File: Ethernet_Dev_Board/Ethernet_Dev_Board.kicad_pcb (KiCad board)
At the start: 2 copper layers, 120 parts, among them J101 Power In, J401 TAG-CONNECT_NL_10-POS_LEGS, Q201 PMV48XPA2R, U101 AZ1117, U102 74AUP1T08GWH, U103 1.2V, U201 WIZNET_W5500, U401 74AUP1T08GWH, U402 ESP32-WROOM-32E, Y201 25MHz, Y301 25MHz

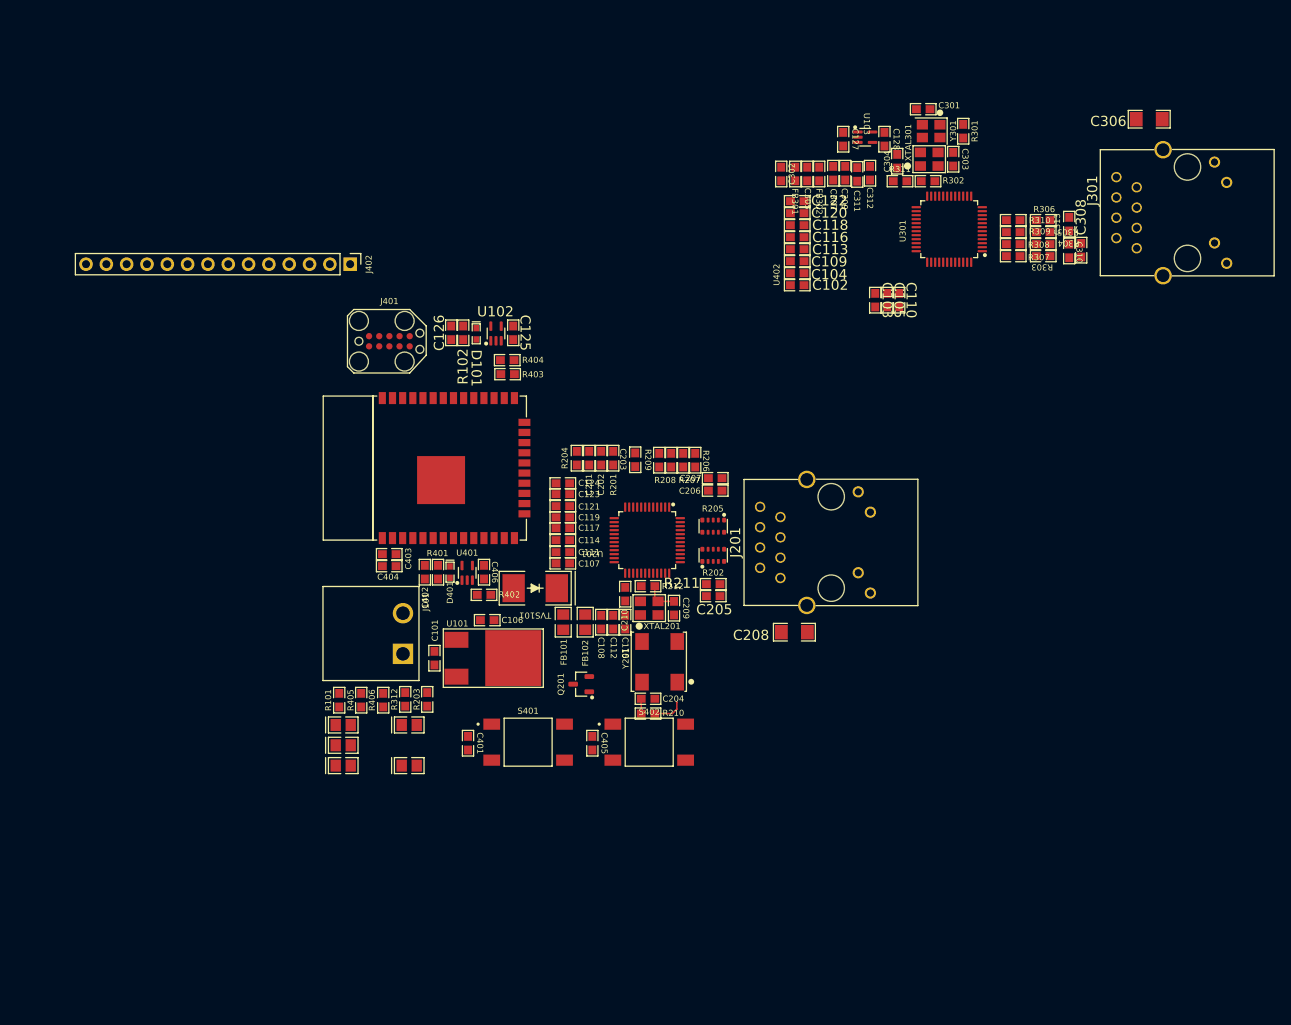
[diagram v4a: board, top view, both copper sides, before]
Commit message: Removed unnecessary nets. Beginning board routing
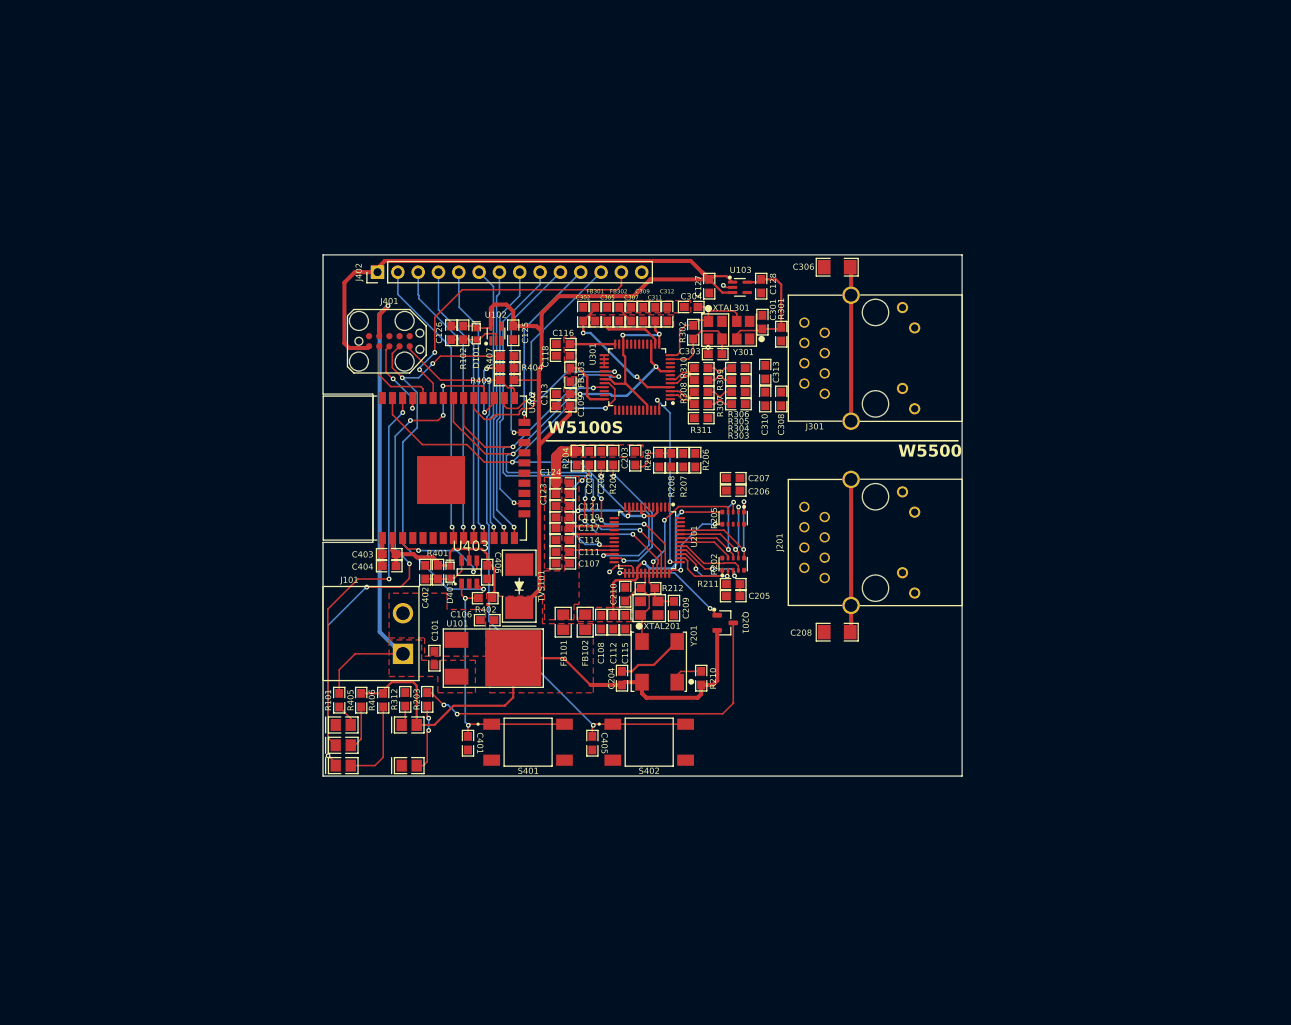
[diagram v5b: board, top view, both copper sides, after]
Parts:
- removed C102, C103, C104, C105: 22uF, RG_Capacitors_SMD:0603
- removed C110, C120, C122: 0.1uF, RG_Capacitors_SMD:0603
- removed U401: 74AUP1T08GWH, RG_TO_SOT_SMD:SOT23-5P65
- added FB103: ~, RG_Resistors_SMD:0603, F.Cu at (108.9, 60.4)
- added R407: 10k, RG_Resistors_SMD:0603, F.Cu at (101.0, 58.0)
- added U403: 74LVC1G11W6, RG_TO_SOT_SMD:SOT23-6, F.Cu at (96.2, 85.0)
- moved C306 43.2 mm to (142.2, 46.9)
- moved R307 43.2 mm to (125.2, 64.0)
- moved R308 43.2 mm to (125.2, 62.5)
- moved R309 43.2 mm to (125.2, 61.0)
- moved R310 43.2 mm to (125.2, 59.5)
- moved U301 43.2 mm to (117.2, 60.6)
- moved J301 43.0 mm to (145.1, 58.2)
- moved R303 42.4 mm to (129.9, 64.0)
- moved R304 42.4 mm to (129.9, 62.5)
- moved R305 42.4 mm to (129.9, 61.0)
- moved R306 42.4 mm to (129.9, 59.5)
- moved C310 42.3 mm to (133.2, 63.4)
- moved C313 42.3 mm to (133.2, 60.0)
- moved C308 41.9 mm to (135.2, 63.4)
- moved R311 38.7 mm to (125.2, 65.8), turned to 180 degrees
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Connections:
- C109 pad 1: +3.3VA -> +3.3V
- C113 pad 1: +3.3VA -> +3.3V
- C116 pad 1: +3.3VA -> +3.3VA2
- C118 pad 1: +3.3VA -> +3.3VA2
- U103 pad 2: GNDS -> GND1
- U301 pad 15: +3.3VA -> +3.3V
- U301 pad 16: GNDS -> GND1
- U301 pad 24: +3.3VD -> +3.3VA2
- U301 pad 36: +3.3VD -> +3.3VA2
- U301 pad 8: +3.3VA -> +3.3V
- XTAL201 pad 2: GNDS -> GND1
- XTAL301 pad 2: GNDS -> GND1
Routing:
- net +3.3V: track 1.85 -> 267.0 mm, vias 0 -> 2
- net IO0: track 0.00 -> 78.8 mm, vias 0 -> 2
- net MOSI: track 0.00 -> 68.8 mm, vias 0 -> 5
- net Net-(U402-IO17): track 0.00 -> 66.8 mm, vias 0 -> 6
- net SCK: track 0.00 -> 63.3 mm, vias 0 -> 5
- net +5V: track 0.00 -> 61.3 mm, vias 0 -> 1
- net MISO: track 0.00 -> 59.9 mm, vias 0 -> 5
- net RST: track 0.00 -> 54.3 mm, vias 0 -> 3
- net Net-(U402-IO22): track 0.00 -> 50.5 mm, vias 0 -> 2
- net Net-(Q201-D): track 0.00 -> 50.2 mm, vias 0 -> 2
- net IO21: track 0.00 -> 38.4 mm, vias 0 -> 2
- net IO32: track 0.00 -> 36.3 mm, vias 0 -> 1
- net IO33: track 0.00 -> 35.6 mm, vias 0 -> 1
- net IO12: track 0.00 -> 35.4 mm, vias 0 -> 1
- net IO25: track 0.00 -> 35.2 mm, vias 0 -> 1
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- added copper zone on F.Cu, net +1.2VD
- added copper zone on F.Cu, net +1.2VO
- added copper zone on F.Cu, net +3.3V
- added copper zone on F.Cu, net +3.3VA
- added copper zone on F.Cu, net +3.3VA2
- added copper zone on F.Cu, net +3.3VD
- added copper zone on F.Cu, net +5V
- added copper zone on F.Cu, net GND1
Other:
- board outline added: 79.9 x 65.2 mm
- board text added: "W5100S"
- board text added: "W5500"

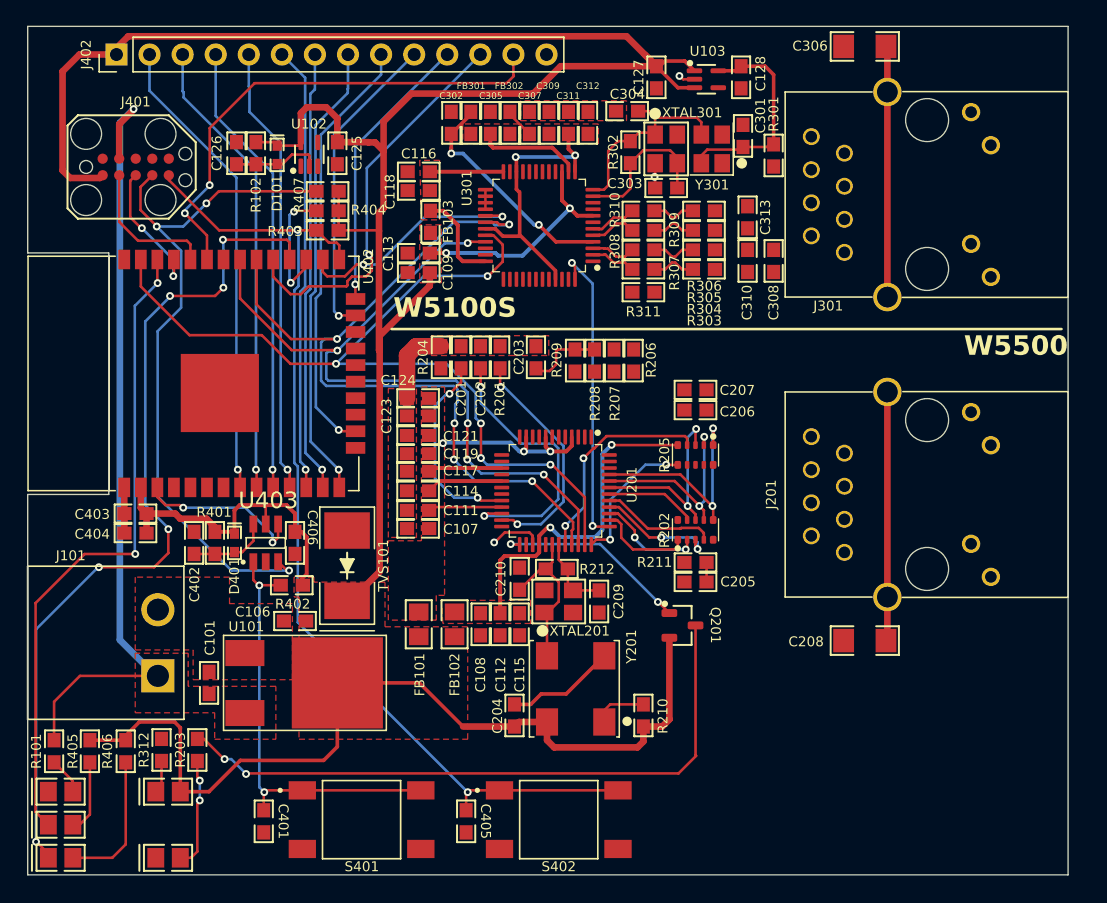
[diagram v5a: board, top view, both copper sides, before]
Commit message: Finished first version of routing the board. Also adjusted some nets
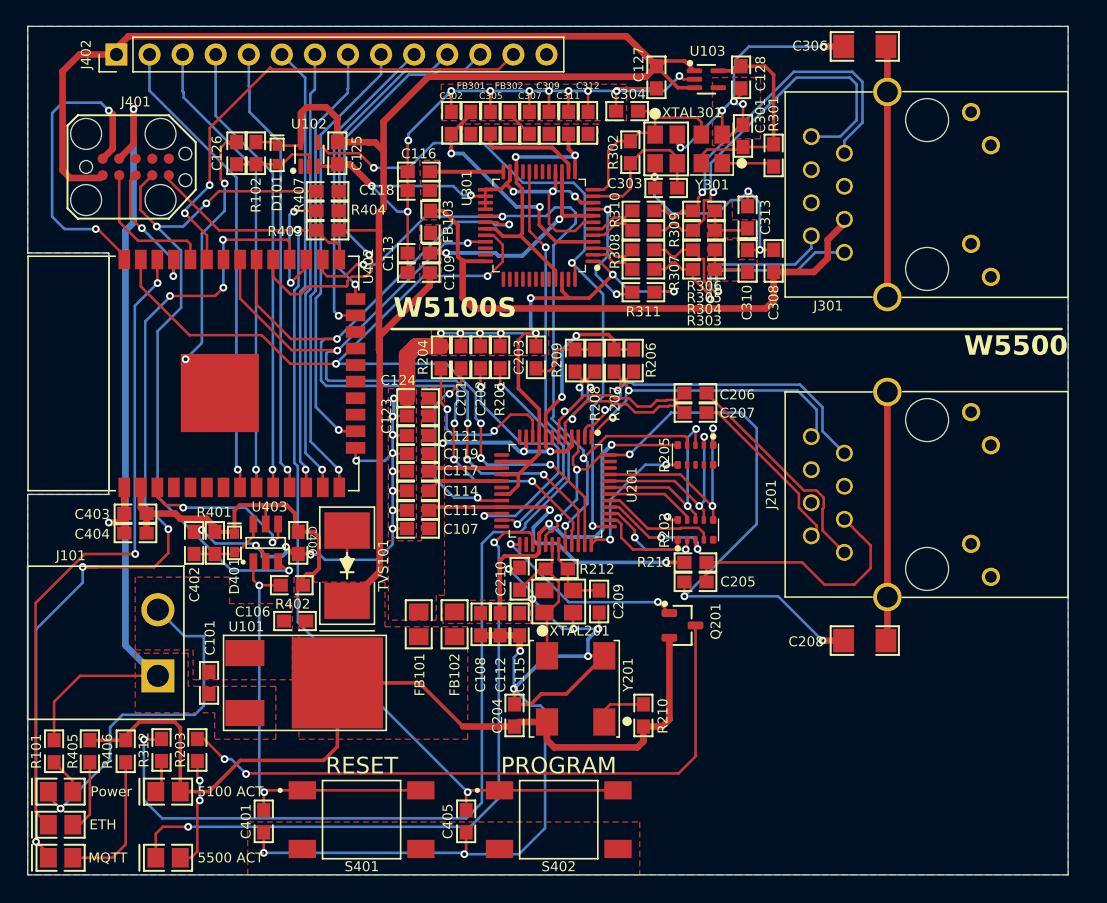
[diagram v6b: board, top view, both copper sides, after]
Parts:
- moved C207 1.75 mm to (129.2, 75.0)
- moved C206 1.31 mm to (129.2, 73.5)
- moved C406 0.25 mm to (98.8, 85.0)
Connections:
- net Net-(J201-RD+) renamed /W5500_Dev/RD+
- net Net-(J201-RD-) renamed /W5500_Dev/RD-
- C308 pad 1: +3.3VA -> +3.3VA2
- J301 pad R3: +3.3VA -> +3.3VA2
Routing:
- net GND1: track 22.9 -> 450.3 mm, vias 2 -> 66
- net Net-(U301-ACTn): track 0.00 -> 86.7 mm, vias 0 -> 2
- net Net-(U201C-ACTLED): track 4.18 -> 53.3 mm, vias 1 -> 2
- net +3.3VA2: track 12.9 -> 50.5 mm
- net +3.3VA: track 30.7 -> 63.7 mm, vias 3 -> 7
- net ETH_EN: track 23.8 -> 53.9 mm, vias 2 -> 3
- net TX_P: track 0.00 -> 27.9 mm, vias 0 -> 2
- net /W5100S_Dev/RX51_N: track 3.38 -> 30.5 mm, vias 0 -> 1
- net SS: track 35.0 -> 61.9 mm
- net /W5100S_Dev/RX51_P: track 3.38 -> 29.4 mm, vias 0 -> 1
- net TX_N: track 0.00 -> 24.0 mm, vias 0 -> 2
- net Net-(J201-CT): track 1.50 -> 19.9 mm
- net /W5500_Dev/RD+: track 0.00 -> 17.3 mm
- net RX_P: track 0.00 -> 16.8 mm, vias 0 -> 2
- net RX_N: track 0.00 -> 16.4 mm, vias 0 -> 2
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- added copper zone on B.Cu, net GND1
- added copper zone on F.Cu, net Net-(C310-Pad1)
- added copper zone on F.Cu, net Net-(C313-Pad1)

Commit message: Minor updates
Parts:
- moved C210 0.25 mm to (115.8, 88.0), turned to -90 degrees
- moved C101 0.10 mm to (92.0, 95.8)
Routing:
- net GND1: track 450.3 -> 464.2 mm, vias 66 -> 65
- net Net-(U201B-TOCAP): track 15.4 -> 21.1 mm
- net SCK: track 63.3 -> 59.0 mm
- net IO32: track 36.3 -> 38.5 mm
- net Net-(U201A-EXRES1): track 13.8 -> 12.7 mm
- net IO33: track 35.6 -> 36.7 mm
- net +3.3V: track 268.9 -> 269.9 mm
- net Net-(U201B-1V20): track 20.7 -> 19.9 mm
- net MOSI: track 68.8 -> 68.2 mm
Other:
- board text added: "+5V"
- board text added: "GND"

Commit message: Converted Board into 4 layers
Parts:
- moved R204 6.80 mm to (116.5, 70.8)
- moved C201 3.75 mm to (115.0, 70.8)
- moved R201 3.75 mm to (118.0, 70.8)
- moved C203 2.50 mm to (119.5, 70.8)
- moved R206 2.25 mm to (126.8, 71.0)
- moved R207 2.25 mm to (125.2, 71.0)
- moved R208 2.25 mm to (123.8, 71.0)
- moved R209 2.25 mm to (122.2, 71.0)
- moved C202 0.75 mm to (113.5, 70.8)
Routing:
- net GND1: track 464.2 -> 416.4 mm, vias 65 -> 68
- net +3.3VA: track 63.3 -> 106.8 mm, vias 7 -> 4
- net SS: track 61.4 -> 75.5 mm, vias 4 -> 7
- net ETH_EN: track 53.9 -> 66.4 mm, vias 3 -> 5
- net +3.3V: track 269.9 -> 279.3 mm
- net Net-(U201B-TOCAP): track 21.1 -> 12.1 mm
- net SCK: track 59.0 -> 67.5 mm, vias 5 -> 4
- net Net-(U201A-EXRES1): track 12.7 -> 5.37 mm, vias 2 -> 0
- net MOSI: track 68.2 -> 74.7 mm, vias 5 -> 6
- net Net-(U201B-1V20): track 19.9 -> 14.4 mm
- net TX_N: track 24.0 -> 29.2 mm
- net MISO: track 59.7 -> 63.3 mm, vias 5 -> 4
- net +3.3VA2: track 50.5 -> 53.5 mm
- net Net-(U201B-RSVD): track 17.2 -> 14.5 mm
- net TX_P: track 27.9 -> 30.4 mm
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- added copper zone on F.Cu, net Net-(C208-Pad1)
- added copper zone on F.Cu, net Net-(C306-Pad1)
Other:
- copper layers 2 -> 4
